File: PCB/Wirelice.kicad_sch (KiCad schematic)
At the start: 35 parts, among them J1 SWD, J2 USB_C_Receptacle_USB2.0, J3 Unified DB, J5 Battery, SW29 SW_Push, U1 nRF52840_holyiot_18010, U2 SRV05-4, U3 TP4056, U4 FS8205, U5 DW01A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

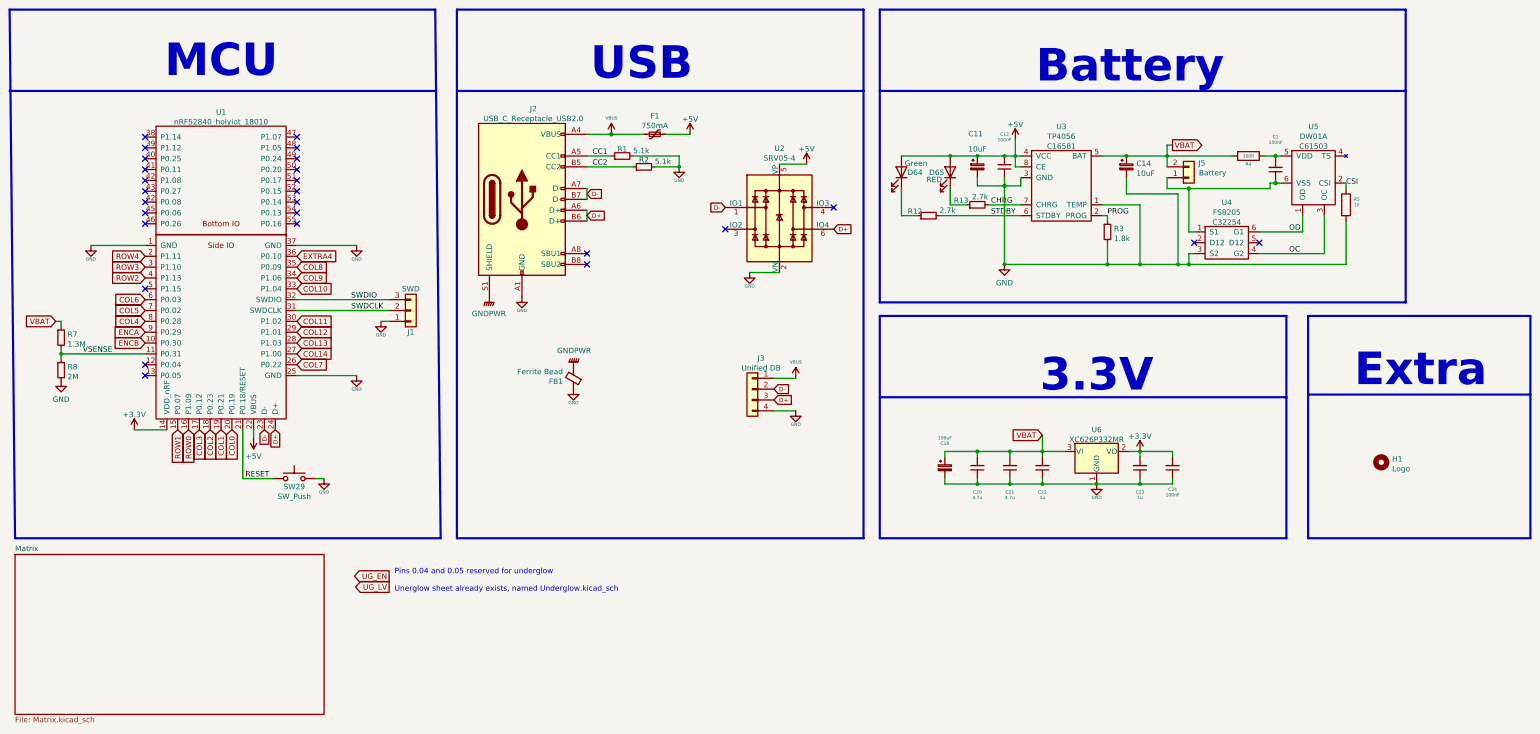
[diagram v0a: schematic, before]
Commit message: Add Plate and Back
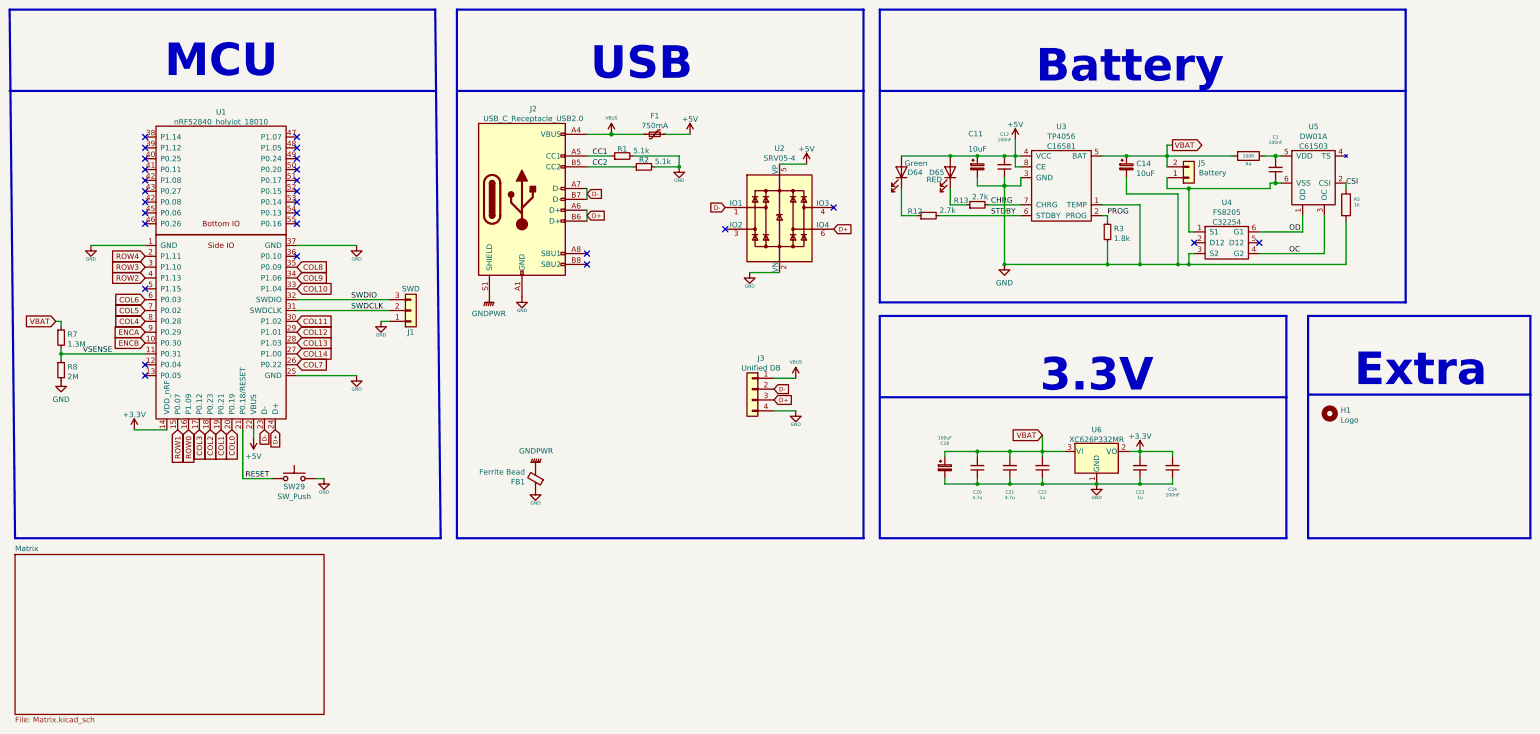
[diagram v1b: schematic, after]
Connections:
- net EXTRA4: no longer names the net of U1.36 (P0.10)
- no-connect marks 27 -> 28
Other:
- note removed: "Pins 0.04 and 0.05 reserved for underglow Unerglow sheet already exists, named Underglow.kicad_sch"
- moved on the sheet: FB1, H1
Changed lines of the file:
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@@
   (no_connect (at 83.82 63.5))
   (no_connect (at 83.82 66.04))
+  (no_connect (at 83.82 73.66))
   (no_connect (at 151.765 73.025))
   (no_connect (at 151.765 75.565))
@@
     (effects (font (size 7.62 7.62) (thickness 1.524) bold) (justify right bottom))
   )
-  (text "Pins 0.04 and 0.05 reserved for underglow\n\nUnerglow sheet already exists, named Underglow.kicad_sch"
-    (at 106.68 152.4 0)
-    (effects (font (size 1.27 1.27)) (justify left bottom))
-  )
   (text "USB" (at 176.53 33.02 180)
     (effects (font (size 7.62 7.62) (thickness 1.524) bold) (justify right bottom))
@@
     )
   )
-  (global_label "EXTRA4" (shape input) (at 83.82 73.66 0) (fields_autoplaced)
-    (effects (font (size 1.27 1.27)) (justify left))
-    (property "Intersheet References" "${INTERSHEET_REFS}" (id 0) (at 93.1274 73.5806 0)
-      (effects (font (size 1.27 1.27)) (justify left) hide)
-    )
-  )
   (global_label "COL8" (shape input) (at 83.82 76.2 0)
     (effects (font (size 1.27 1.27)) (justify left))
@@
     (property "Intersheet References" "${INTERSHEET_REFS}" (id 0) (at -266.065 154.94 0)
       (effects (font (size 1.27 1.27)) hide)
-    )
-  )
-  (global_label "UG_EN" (shape output) (at 105.41 148.59 180) (fields_autoplaced)
-    (effects (font (size 1.27 1.27)) (justify right))
-    (property "Intersheet References" "${INTERSHEET_REFS}" (id 0) (at 96.9493 148.6694 0)
-      (effects (font (size 1.27 1.27)) (justify right) hide)
-    )
-  )
-  (global_label "UG_LV" (shape output) (at 105.41 151.13 180) (fields_autoplaced)
-    (effects (font (size 1.27 1.27)) (justify right))
-    (property "Intersheet References" "${INTERSHEET_REFS}" (id 0) (at 97.3121 151.0506 0)
-      (effects (font (size 1.27 1.27)) (justify right) hide)
     )
   )
@@
     (pin "1")
   )
-  (symbol (lib_id "power:GNDPWR") (at 148.59 99.695 180) (unit 1)
-    (in_bom yes) (on_board yes) (fields_autoplaced)
-    (property "Reference" "#PWR0107" (id 0) (at 148.59 94.615 0)
-      (effects (font (size 1.27 1.27)) hide)
-    )
-    (property "Value" "GNDPWR" (id 1) (at 148.717 95.777 0))
-    (property "Footprint" "" (id 2) (at 148.59 98.425 0)
-      (effects (font (size 1.27 1.27)) hide)
-    )
-    (property "Datasheet" "" (id 3) (at 148.59 98.425 0)
+  (symbol (lib_id "power:GNDPWR") (at 139.7 123.19 180) (unit 1)
+    (in_bom yes) (on_board yes) (fields_autoplaced)
+    (property "Reference" "#PWR0107" (id 0) (at 139.7 118.11 0)
+      (effects (font (size 1.27 1.27)) hide)
+    )
+    (property "Value" "GNDPWR" (id 1) (at 139.827 119.272 0))
+    (property "Footprint" "" (id 2) (at 139.7 121.92 0)
+      (effects (font (size 1.27 1.27)) hide)
+    )
+    (property "Datasheet" "" (id 3) (at 139.7 121.92 0)
       (effects (font (size 1.27 1.27)) hide)
     )
@@
     (pin "1")
   )
-  (symbol (lib_id "power:GND") (at 148.59 104.775 0) (unit 1)
-    (in_bom yes) (on_board yes)
-    (property "Reference" "#PWR0108" (id 0) (at 148.59 111.125 0)
-      (effects (font (size 1.27 1.27)) hide)
-    )
-    (property "Value" "GND" (id 1) (at 148.59 107.95 0)
-      (effects (font (size 0.762 0.762)))
-    )
-    (property "Footprint" "" (id 2) (at 148.59 104.775 0)
-      (effects (font (size 1.27 1.27)) hide)
-    )
-    (property "Datasheet" "" (id 3) (at 148.59 104.775 0)
+  (symbol (lib_id "power:GND") (at 139.7 128.27 0) (unit 1)
+    (in_bom yes) (on_board yes)
+    (property "Reference" "#PWR0108" (id 0) (at 139.7 134.62 0)
+      (effects (font (size 1.27 1.27)) hide)
+    )
+    (property "Value" "GND" (id 1) (at 139.7 131.445 0)
+      (effects (font (size 0.762 0.762)))
+    )
+    (property "Footprint" "" (id 2) (at 139.7 128.27 0)
+      (effects (font (size 1.27 1.27)) hide)
+    )
+    (property "Datasheet" "" (id 3) (at 139.7 128.27 0)
       (effects (font (size 1.27 1.27)) hide)
     )
@@
     (pin "2")
   )
-  (symbol (lib_id "Mechanical:MountingHole") (at 337.82 121.92 0) (unit 1)
+  (symbol (lib_id "Mechanical:MountingHole") (at 325.755 110.49 0) (unit 1)
     (in_bom no) (on_board yes) (fields_autoplaced)
-    (property "Reference" "H1" (id 0) (at 340.3601 121.1591 0)
+    (property "Reference" "H1" (id 0) (at 328.2951 109.7291 0)
       (effects (font (size 1.27 1.27)) (justify left))
     )
-    (property "Value" "Logo" (id 1) (at 340.3601 123.4578 0)
+    (property "Value" "Logo" (id 1) (at 328.2951 112.0278 0)
       (effects (font (size 1.27 1.27)) (justify left))
     )
-    (property "Footprint" "sleep-lib:logo-large-CU" (id 2) (at 337.82 121.92 0)
-      (effects (font (size 1.27 1.27)) hide)
-    )
-    (property "Datasheet" "~" (id 3) (at 337.82 121.92 0)
+    (property "Footprint" "sleep-lib:logo-large-CU" (id 2) (at 325.755 110.49 0)
+      (effects (font (size 1.27 1.27)) hide)
+    )
+    (property "Datasheet" "~" (id 3) (at 325.755 110.49 0)
       (effects (font (size 1.27 1.27)) hide)
     )
@@
     (pin "2")
   )
-  (symbol (lib_id "Device:Ferrite_Bead_Small") (at 148.59 102.235 180) (unit 1)
-    (in_bom yes) (on_board yes) (fields_autoplaced)
-    (property "Reference" "FB1" (id 0) (at 146.1261 102.9959 0)
+  (symbol (lib_id "Device:Ferrite_Bead_Small") (at 139.7 125.73 180) (unit 1)
+    (in_bom yes) (on_board yes) (fields_autoplaced)
+    (property "Reference" "FB1" (id 0) (at 137.2361 126.4909 0)
       (effects (font (size 1.27 1.27)) (justify left))
     )
-    (property "Value" "Ferrite Bead" (id 1) (at 146.1261 100.6972 0)
+    (property "Value" "Ferrite Bead" (id 1) (at 137.2361 124.1922 0)
       (effects (font (size 1.27 1.27)) (justify left))
     )
-    (property "Footprint" "Inductor_SMD:L_0805_2012Metric" (id 2) (at 150.368 102.235 90)
-      (effects (font (size 1.27 1.27)) hide)
-    )
-    (property "Datasheet" "~" (id 3) (at 148.59 102.235 0)
-      (effects (font (size 1.27 1.27)) hide)
-    )
-    (property "LCSC" "C1017" (id 4) (at 148.59 102.235 0)
-      (effects (font (size 1.27 1.27)) hide)
-    )
+    (property "Footprint" "Inductor_SMD:L_0805_2012Metric" (id 2) (at 141.478 125.73 90)
+      (effects (font (size 1.27 1.27)) hide)
+    )
+    (property "Datasheet" "~" (id 3) (at 139.7 125.73 0)
+      (effects (font (size 1.27 1.27)) hide)
+    )
+    (property "LCSC" "C1017" (id 4) (at 139.7 125.73 0)
+      (effects (font (size 1.27 1.27)) hide)
+    )

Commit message: Updated stuff
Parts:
- J3: Part Number (none) -> SM04B-SRSS-TB(LF)(SN)
- J5: Part Number (none) -> S2B-PH-SM4-TB; now in the parts list
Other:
- moved on the sheet: FB1, J3
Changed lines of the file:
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@@
-    (stroke (width 0) (type solid) (color 0 0 0 0))
-  )
-  (wire (pts (xy 195.58 102.235) (xy 200.66 102.235))
-    (stroke (width 0) (type solid) (color 0 0 0 0))
-  )
-  (wire (pts (xy 195.58 109.855) (xy 200.66 109.855))
     (stroke (width 0) (type solid) (color 0 0 0 0))
   )
   (wire (pts (xy 196.85 52.07) (xy 203.2 52.07))
+    (stroke (width 0) (type solid) (color 0 0 0 0))
+  )
+  (wire (pts (xy 196.85 91.44) (xy 201.93 91.44))
+    (stroke (width 0) (type solid) (color 0 0 0 0))
+  )
+  (wire (pts (xy 196.85 99.06) (xy 201.93 99.06))
     (stroke (width 0) (type solid) (color 0 0 0 0))
   )
@@
     )
   )
-  (global_label "D-" (shape input) (at 195.58 104.775 0)
+  (global_label "D-" (shape input) (at 196.85 93.98 0)
     (effects (font (size 1.016 1.016)) (justify left))
-    (property "Intersheet References" "${INTERSHEET_REFS}" (id 0) (at 449.58 456.565 0)
+    (property "Intersheet References" "${INTERSHEET_REFS}" (id 0) (at 450.85 445.77 0)
       (effects (font (size 1.016 1.016)) hide)
     )
   )
-  (global_label "D+" (shape input) (at 195.58 107.315 0)
+  (global_label "D+" (shape input) (at 196.85 96.52 0)
     (effects (font (size 1.016 1.016)) (justify left))
-    (property "Intersheet References" "${INTERSHEET_REFS}" (id 0) (at -81.28 -244.475 0)
+    (property "Intersheet References" "${INTERSHEET_REFS}" (id 0) (at -80.01 -255.27 0)
       (effects (font (size 1.016 1.016)) hide)
     )
@@
     (pin "1")
   )
-  (symbol (lib_id "power:VBUS") (at 200.66 102.235 0) (unit 1)
-    (in_bom yes) (on_board yes)
-    (property "Reference" "#PWR029" (id 0) (at 200.66 106.045 0)
-      (effects (font (size 1.27 1.27)) hide)
-    )
-    (property "Value" "VBUS" (id 1) (at 200.66 98.425 0)
-      (effects (font (size 0.762 0.762)))
-    )
-    (property "Footprint" "" (id 2) (at 200.66 102.235 0)
-      (effects (font (size 1.27 1.27)) hide)
-    )
-    (property "Datasheet" "" (id 3) (at 200.66 102.235 0)
+  (symbol (lib_id "power:VBUS") (at 201.93 91.44 0) (unit 1)
+    (in_bom yes) (on_board yes)
+    (property "Reference" "#PWR029" (id 0) (at 201.93 95.25 0)
+      (effects (font (size 1.27 1.27)) hide)
+    )
+    (property "Value" "VBUS" (id 1) (at 201.93 87.63 0)
+      (effects (font (size 0.762 0.762)))
+    )
+    (property "Footprint" "" (id 2) (at 201.93 91.44 0)
+      (effects (font (size 1.27 1.27)) hide)
+    )
+    (property "Datasheet" "" (id 3) (at 201.93 91.44 0)
       (effects (font (size 1.27 1.27)) hide)
     )
@@
     (pin "1")
   )
-  (symbol (lib_id "power:GNDPWR") (at 139.7 123.19 180) (unit 1)
-    (in_bom yes) (on_board yes) (fields_autoplaced)
-    (property "Reference" "#PWR0107" (id 0) (at 139.7 118.11 0)
-      (effects (font (size 1.27 1.27)) hide)
-    )
-    (property "Value" "GNDPWR" (id 1) (at 139.827 119.272 0))
-    (property "Footprint" "" (id 2) (at 139.7 121.92 0)
-      (effects (font (size 1.27 1.27)) hide)
-    )
-    (property "Datasheet" "" (id 3) (at 139.7 121.92 0)
+  (symbol (lib_id "power:GNDPWR") (at 166.37 88.9 180) (unit 1)
+    (in_bom yes) (on_board yes) (fields_autoplaced)
+    (property "Reference" "#PWR0107" (id 0) (at 166.37 83.82 0)
+      (effects (font (size 1.27 1.27)) hide)
+    )
+    (property "Value" "GNDPWR" (id 1) (at 166.497 84.982 0))
+    (property "Footprint" "" (id 2) (at 166.37 87.63 0)
+      (effects (font (size 1.27 1.27)) hide)
+    )
+    (property "Datasheet" "" (id 3) (at 166.37 87.63 0)
       (effects (font (size 1.27 1.27)) hide)
     )
@@
     (pin "1")
   )
-  (symbol (lib_id "power:GND") (at 139.7 128.27 0) (unit 1)
-    (in_bom yes) (on_board yes)
-    (property "Reference" "#PWR0108" (id 0) (at 139.7 134.62 0)
-      (effects (font (size 1.27 1.27)) hide)
-    )
-    (property "Value" "GND" (id 1) (at 139.7 131.445 0)
-      (effects (font (size 0.762 0.762)))
-    )
-    (property "Footprint" "" (id 2) (at 139.7 128.27 0)
-      (effects (font (size 1.27 1.27)) hide)
-    )
-    (property "Datasheet" "" (id 3) (at 139.7 128.27 0)
+  (symbol (lib_id "power:GND") (at 166.37 93.98 0) (unit 1)
+    (in_bom yes) (on_board yes)
+    (property "Reference" "#PWR0108" (id 0) (at 166.37 100.33 0)
+      (effects (font (size 1.27 1.27)) hide)
+    )
+    (property "Value" "GND" (id 1) (at 166.37 97.155 0)
+      (effects (font (size 0.762 0.762)))
+    )
+    (property "Footprint" "" (id 2) (at 166.37 93.98 0)
+      (effects (font (size 1.27 1.27)) hide)
+    )
+    (property "Datasheet" "" (id 3) (at 166.37 93.98 0)
       (effects (font (size 1.27 1.27)) hide)
     )
@@
     (pin "1")
   )
-  (symbol (lib_id "power:GND") (at 200.66 109.855 0) (unit 1)
-    (in_bom yes) (on_board yes)
-    (property "Reference" "#PWR030" (id 0) (at 200.66 116.205 0)
-      (effects (font (size 1.27 1.27)) hide)
-    )
-    (property "Value" "GND" (id 1) (at 200.66 113.03 0)
-      (effects (font (size 0.762 0.762)))
-    )
-    (property "Footprint" "" (id 2) (at 200.66 109.855 0)
-      (effects (font (size 1.27 1.27)) hide)
-    )
-    (property "Datasheet" "" (id 3) (at 200.66 109.855 0)
+  (symbol (lib_id "power:GND") (at 201.93 99.06 0) (unit 1)
+    (in_bom yes) (on_board yes)
+    (property "Reference" "#PWR030" (id 0) (at 201.93 105.41 0)
+      (effects (font (size 1.27 1.27)) hide)
+    )
+    (property "Value" "GND" (id 1) (at 201.93 102.235 0)
+      (effects (font (size 0.762 0.762)))
+    )
+    (property "Footprint" "" (id 2) (at 201.93 99.06 0)
+      (effects (font (size 1.27 1.27)) hide)
+    )
+    (property "Datasheet" "" (id 3) (at 201.93 99.06 0)
       (effects (font (size 1.27 1.27)) hide)
     )
@@
     (pin "2")
   )
-  (symbol (lib_id "Device:Ferrite_Bead_Small") (at 139.7 125.73 180) (unit 1)
-    (in_bom yes) (on_board yes) (fields_autoplaced)
-    (property "Reference" "FB1" (id 0) (at 137.2361 126.4909 0)
-      (effects (font (size 1.27 1.27)) (justify left))
-    )
-    (property "Value" "Ferrite Bead" (id 1) (at 137.2361 124.1922 0)
-      (effects (font (size 1.27 1.27)) (justify left))
-    )
-    (property "Footprint" "Inductor_SMD:L_0805_2012Metric" (id 2) (at 141.478 125.73 90)
-      (effects (font (size 1.27 1.27)) hide)
-    )
-    (property "Datasheet" "~" (id 3) (at 139.7 125.73 0)
-      (effects (font (size 1.27 1.27)) hide)
-    )
-    (property "LCSC" "C1017" (id 4) (at 139.7 125.73 0)
+  (symbol (lib_id "Device:Ferrite_Bead_Small") (at 166.37 91.44 180) (unit 1)
+    (in_bom yes) (on_board yes) (fields_autoplaced)
+    (property "Reference" "FB1" (id 0) (at 163.9061 92.2009 0)
+      (effects (font (size 1.27 1.27)) (justify left))
+    )
+    (property "Value" "Ferrite Bead" (id 1) (at 163.9061 89.9022 0)
+      (effects (font (size 1.27 1.27)) (justify left))
+    )
+    (property "Footprint" "Inductor_SMD:L_0805_2012Metric" (id 2) (at 168.148 91.44 90)
+      (effects (font (size 1.27 1.27)) hide)
+    )
+    (property "Datasheet" "~" (id 3) (at 166.37 91.44 0)
+      (effects (font (size 1.27 1.27)) hide)
+    )
+    (property "LCSC" "C1017" (id 4) (at 166.37 91.44 0)
       (effects (font (size 1.27 1.27)) hide)
     )
@@
   )
   (symbol (lib_id "Connector_Generic:Conn_01x02") (at 292.735 55.245 0) (mirror x) (unit 1)
-    (in_bom no) (on_board yes)
+    (in_bom yes) (on_board yes)
     (property "Reference" "J5" (id 0) (at 295.783 51.8118 0))
     (property "Value" "Battery" (id 1) (at 298.323 54.1105 0))
@@
     )
     (property "Datasheet" "~" (id 3) (at 292.735 55.245 0)
+      (effects (font (size 1.27 1.27)) hide)
+    )
+    (property "Part Number" "S2B-PH-SM4-TB" (id 4) (at 292.735 55.245 0)
       (effects (font (size 1.27 1.27)) hide)
     )
@@
     (pin "3")
   )
-  (symbol (lib_id "Connector_Generic:Conn_01x04") (at 190.5 104.775 0) (mirror y) (unit 1)
-    (in_bom yes) (on_board yes) (fields_autoplaced)
-    (property "Reference" "J3" (id 0) (at 192.532 97.5318 0))
-    (property "Value" "Unified DB" (id 1) (at 192.532 99.8305 0))
-    (property "Footprint" "Connector_JST:JST_SH_SM04B-SRSS-TB_1x04-1MP_P1.00mm_Horizontal" (id 2) (at 190.5 104.775 0)
-      (effects (font (size 1.27 1.27)) hide)
-    )
-    (property "Datasheet" "~" (id 3) (at 190.5 104.775 0)
-      (effects (font (size 1.27 1.27)) hide)
-    )
-    (property "LCSC" "C160404" (id 4) (at 190.5 104.775 0)
-      (effects (font (size 1.27 1.27)) hide)
-    )
+  (symbol (lib_id "Connector_Generic:Conn_01x04") (at 191.77 93.98 0) (mirror y) (unit 1)
+    (in_bom yes) (on_board yes) (fields_autoplaced)
+    (property "Reference" "J3" (id 0) (at 193.802 86.7368 0))
+    (property "Value" "Unified DB" (id 1) (at 193.802 89.0355 0))
+    (property "Footprint" "Connector_JST:JST_SH_SM04B-SRSS-TB_1x04-1MP_P1.00mm_Horizontal" (id 2) (at 191.77 93.98 0)
+      (effects (font (size 1.27 1.27)) hide)
+    )
+    (property "Datasheet" "~" (id 3) (at 191.77 93.98 0)
+      (effects (font (size 1.27 1.27)) hide)
+    )
+    (property "LCSC" "C160404" (id 4) (at 191.77 93.98 0)
+      (effects (font (size 1.27 1.27)) hide)
+    )
+    (property "Part Number" "SM04B-SRSS-TB(LF)(SN)" (id 5) (at 191.77 93.98 0)
+      (effects (font (size 1.27 1.27)) hide)
+    )
